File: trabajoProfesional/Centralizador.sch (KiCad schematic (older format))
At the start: 0 parts

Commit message: Placa uno terminada!
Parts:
- added IC?: HV7361GA-G, BGA22C50P9X14_500X700X105, symbol HV7361GA-G:HV7361GA-G
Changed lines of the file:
@@
 $Descr A4 11693 8268
 encoding utf-8
-Sheet 1 5
+Sheet 5 5
 Title ""
 Date ""
@@
 Comment4 ""
 $EndDescr
+$Comp
+L HV7361GA-G:HV7361GA-G IC?
+U 1 1 5FFE4A75
+P 3900 2200
+F 0 "IC?" H 4450 2465 50  0000 C CNN
+F 1 "HV7361GA-G" H 4450 2374 50  0000 C CNN
+F 2 "BGA22C50P9X14_500X700X105" H 4850 2300 50  0001 L CNN
+F 3 "http://ww1.microchip.com/downloads/en/DeviceDoc/20005570C.pdf" H 4850 2200 50  0001 L CNN
+F 4 "Power Management Specialized - PMIC 1-Ch +/-100V 2.5A 2/3-Lev AC Coupled Pulser w/T-R Switch" H 4850 2100 50  0001 L CNN "Description"
+F 5 "1.05" H 4850 2000 50  0001 L CNN "Height"
+F 6 "579-HV7361GA-G" H 4850 1900 50  0001 L CNN "Mouser Part Number"
+F 7 "https://www.mouser.co.uk/ProductDetail/Microchip-Technology/HV7361GA-G?qs=NoqMqJKvPFJ98Yl1cb744A%3D%3D" H 4850 1800 50  0001 L CNN "Mouser Price/Stock"
+F 8 "Microchip" H 4850 1700 50  0001 L CNN "Manufacturer_Name"
+F 9 "HV7361GA-G" H 4850 1600 50  0001 L CNN "Manufacturer_Part_Number"
+	1    3900 2200
+	1    0    0    -1
+$EndComp
 $EndSCHEMATC

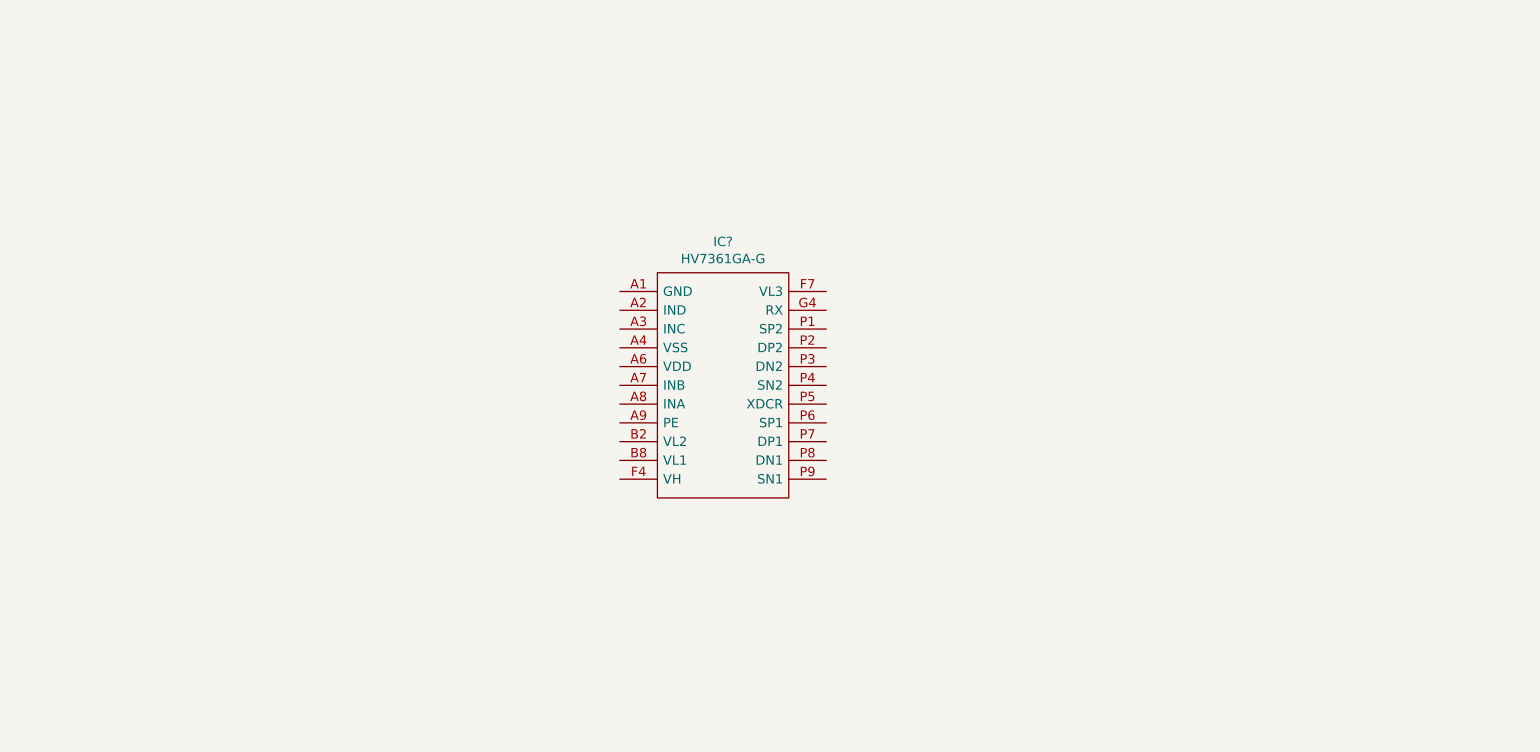
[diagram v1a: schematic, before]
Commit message: agregamos los dos circuitos que nos faltaban, cargador y centralizador
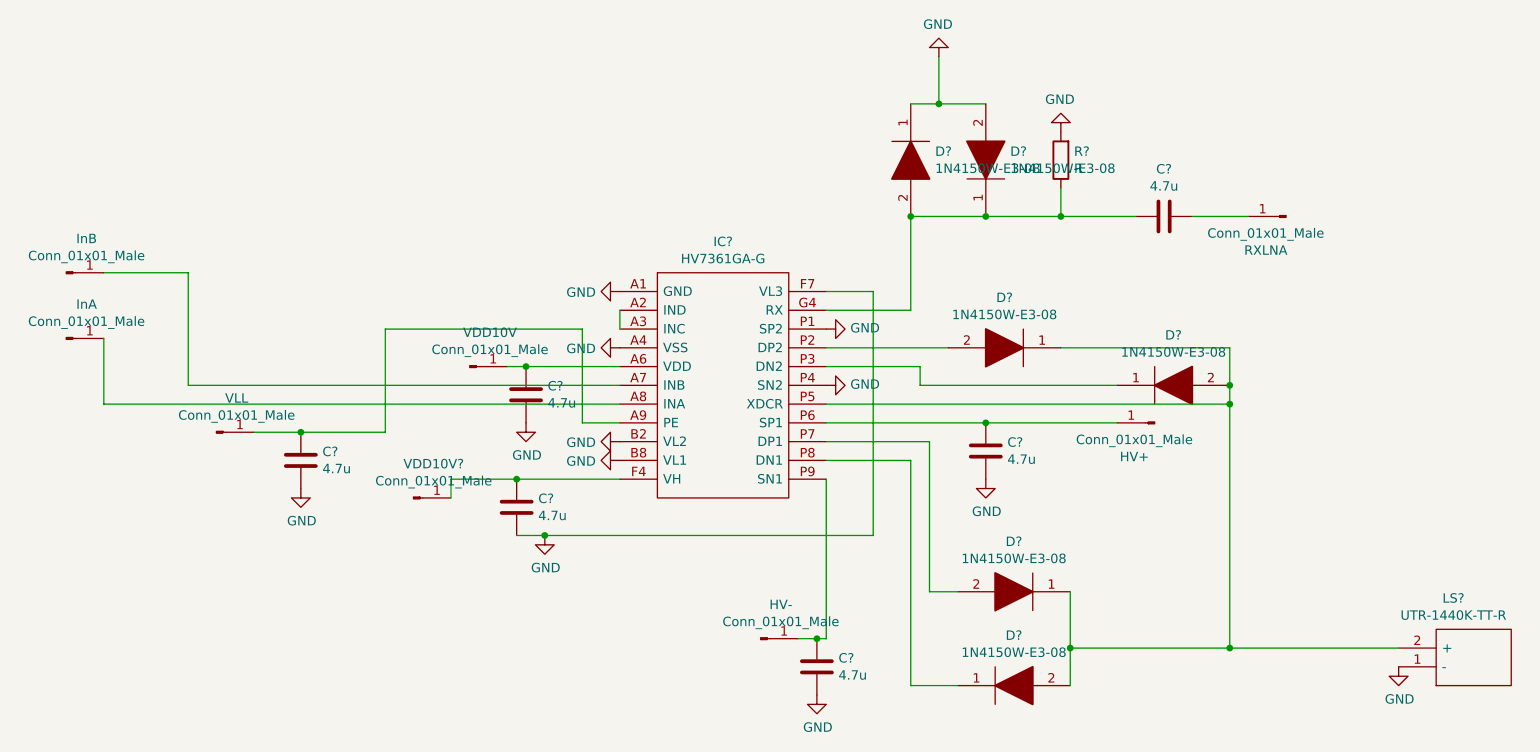
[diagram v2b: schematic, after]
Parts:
- added C? (x6): 4.7u, symbol Device:C
- added D? (x6): 1N4150W-E3-08, SOD3716X135N, symbol Diodo1N4150W-e3-08:1N4150W-E3-08
- added HV+, HV-, InA, InB, RXLNA, VDD10V, VDD10V?, VLL: Conn_01x01_Male, symbol Connector:Conn_01x01_Male
- added LS?: UTR-1440K-TT-R, UTR1440KTTR, symbol UTR-1440K-TT-R:UTR-1440K-TT-R
- added R?: R, symbol Device:R
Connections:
- net GND: now reaches IC?.A1 (GND)
- net GND: now also IC?.A4 (VSS), IC?.B2 (VL2), IC?.B8 (VL1), IC?.F7 (VL3), IC?.P1 (SP2), IC?.P4 (SN2), C?.2, C?.2, C?.2, C?.2, C?.2, D?.1, D?.2, LS?.1 (-), R?.2
- net at IC?.A2 (IND): now also IC?.A3 (INC)
- net at IC?.A6 (VDD): now also C?.1, VDD10V.1 (Pin_1)
- net at IC?.A7 (INB): now also InB.1 (Pin_1)
- net at IC?.A8 (INA): now also InA.1 (Pin_1)
- net at IC?.A9 (PE): now also C?.1, VLL.1 (Pin_1)
- net at IC?.F4 (VH): now also C?.1, VDD10V?.1 (Pin_1)
- net at IC?.G4 (RX): now also C?.2, D?.1, D?.2, R?.1
- net at IC?.P2 (DP2): now also D?.2
- net at IC?.P3 (DN2): now also D?.1
- net at IC?.P5 (XDCR): now also D?.1, D?.1, D?.2, D?.2, LS?.2 (+)
- net at IC?.P6 (SP1): now also C?.1, HV+.1 (Pin_1)
- net at IC?.P7 (DP1): now also D?.2
- net at IC?.P8 (DN1): now also D?.1
- net at IC?.P9 (SN1): now also C?.1, HV-.1 (Pin_1)
- new net: C?.1, RXLNA.1 (Pin_1)

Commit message: el paso previo a agregar todos los componentes de las otras placas
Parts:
- C20, C21, C22, C23, C24, C25: renamed from C?; footprint (none) -> Capacitor_SMD:C_0805_2012Metric
- D10, D11, D6, D7, D8, D9: renamed from D?; footprint SOD3716X135N -> Diodo1N4150W-e3-08:SOD3716X135N
- HV+2: renamed from HV+; footprint (none) -> TestPoint:TestPoint_Pad_D4.0mm
- HV-2: renamed from HV-; footprint (none) -> TestPoint:TestPoint_Pad_D4.0mm
- IC2: renamed from IC?; footprint BGA22C50P9X14_500X700X105 -> HV7361GA-G:BGA22C50P9X14_500X700X105
- InA1: renamed from InA; footprint (none) -> TestPoint:TestPoint_Pad_D3.0mm
- InB1: renamed from InB; footprint (none) -> TestPoint:TestPoint_Pad_D3.0mm
- LS1: renamed from LS?; footprint UTR1440KTTR -> UTR-1440K-TT-R:UTR1440KTTR
- R9: renamed from R?; footprint (none) -> Resistor_SMD:R_0805_2012Metric
- RXLNA1: renamed from RXLNA; footprint (none) -> TestPoint:TestPoint_Pad_D4.0mm
- VDD10V1: renamed from VDD10V?; footprint (none) -> TestPoint:TestPoint_Pad_D3.0mm
- VDD10V2: renamed from VDD10V; footprint (none) -> TestPoint:TestPoint_Pad_D3.0mm
- VLL1: renamed from VLL; footprint (none) -> TestPoint:TestPoint_Pad_D3.0mm
